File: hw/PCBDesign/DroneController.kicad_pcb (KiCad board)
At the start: 4 copper layers, 100 x 50 mm, 220 parts, among them J1 SerialDebug, J10 SW_B, J11 YTrim, J12 SW_C, J13 TTrim, J14 SW_D, J2 USB_B_Micro, J3 ExtBatt, J4 Conn_ARM_JTAG_SWD_10, J5 EncoderConn, J6 JoystickConn, J7 PTrim, J8 SW_A, J9 RTrim, Q1 MMBT3904, Q2 2N7002, Q3 2N7002, Q4 LBSS84LT1G, Q5 LBSS84LT1G, SW13 Key_User, SW15 Key_nRESET, SW17 Key_nBOOT, U1 74HC165, U11 74HC595, U13 STM32F446RETx, U14 RN4871, U2 74HC165, U3 74HC165, U4 AT25SF081, U5 AT24C256, U6 NRF24L01_Breakout, U7 TP4056, U8 AMS1117-3.3, Y1 8MHz Crystal

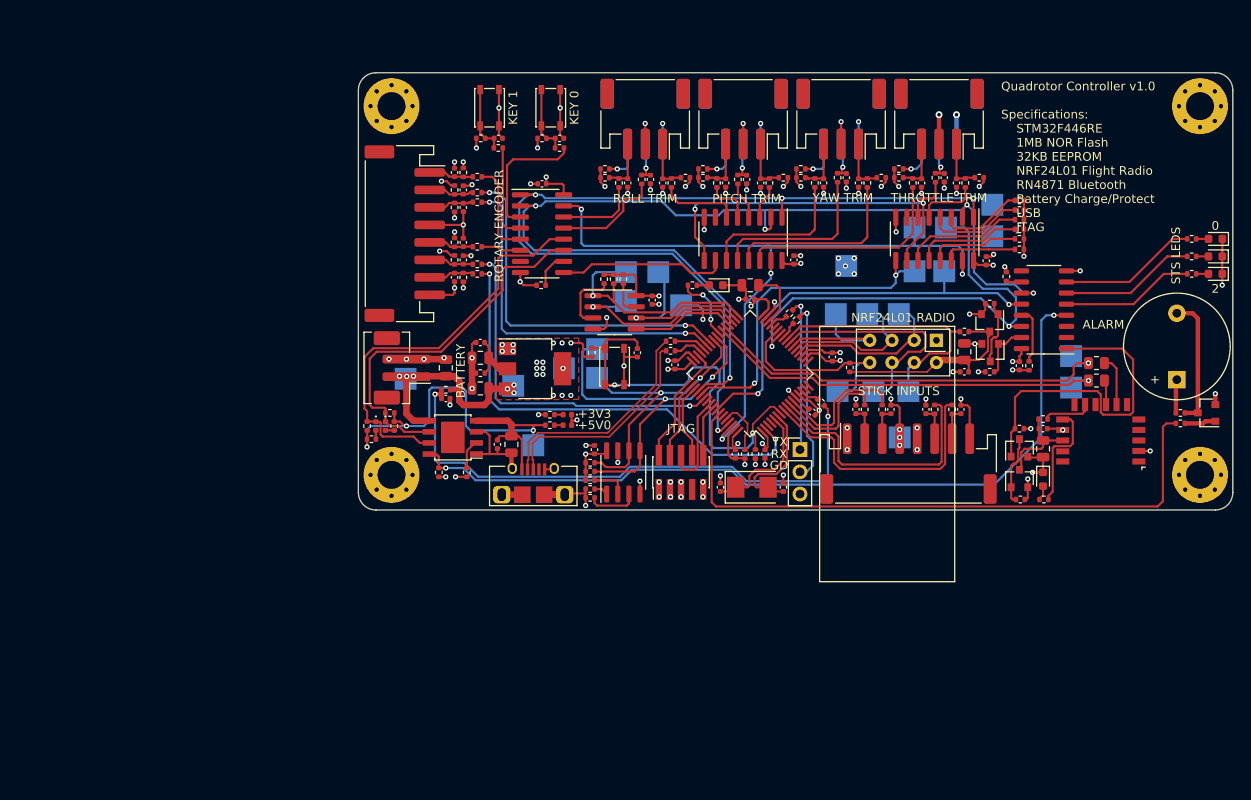
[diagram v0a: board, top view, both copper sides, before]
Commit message: Start working on PCB rev 2.0
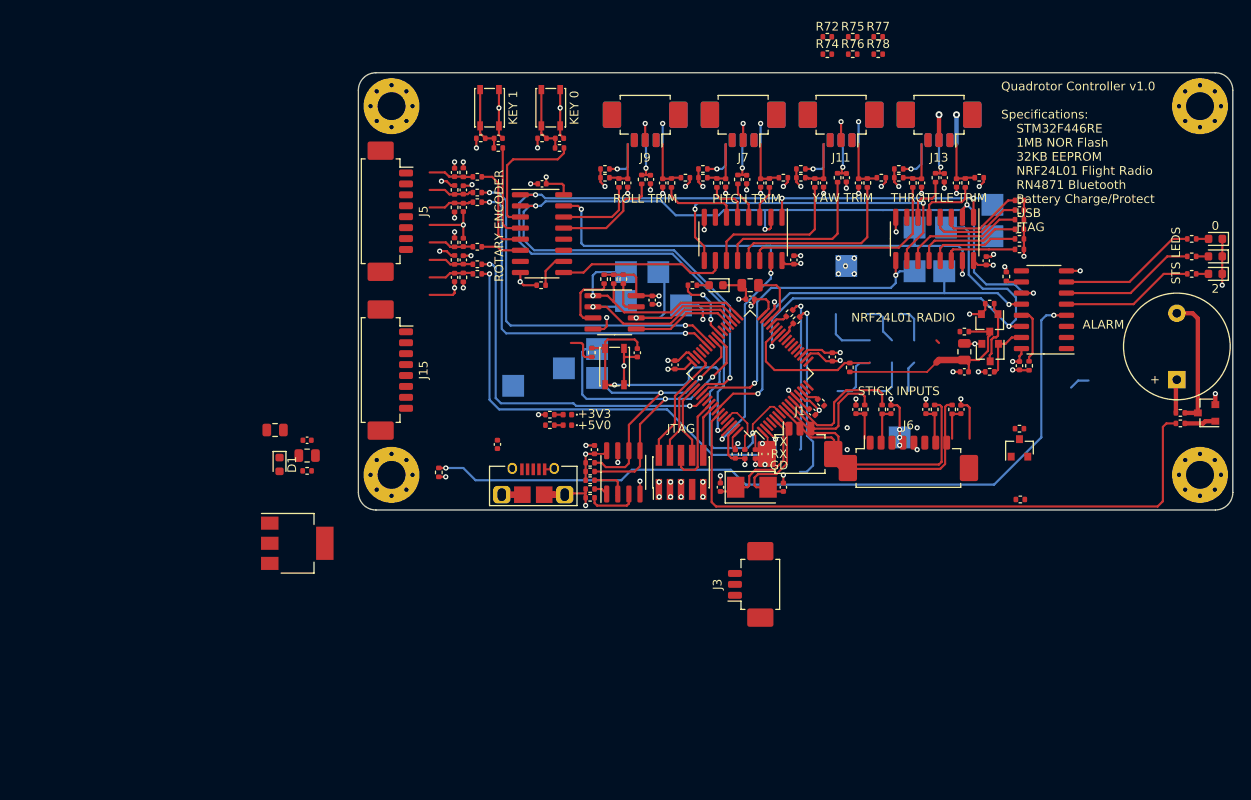
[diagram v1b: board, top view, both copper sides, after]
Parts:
- removed C36: 1uF, Capacitor_SMD:C_0805_2012Metric
- removed C38: 4.7uF, Capacitor_SMD:C_0805_2012Metric
- removed C40, C58: 100n, Capacitor_SMD:C_0402_1005Metric
- removed C59: 10uF, Capacitor_SMD:C_0805_2012Metric
- removed D2: LED_CHG, LED_SMD:LED_0402_1005Metric
- removed D7: BT_ON, LED_SMD:LED_0603_1608Metric
- removed Q4: LBSS84LT1G, Package_TO_SOT_SMD:SOT-23
- removed R100, R79: 10k, Resistor_SMD:R_0402_1005Metric
- removed R101: 560, Resistor_SMD:R_0402_1005Metric
- removed R52, R54: 33, Resistor_SMD:R_0402_1005Metric
- removed R80, R81: 1.5k, Resistor_SMD:R_0402_1005Metric
- removed R82, R83, R84: 100k, Resistor_SMD:R_0402_1005Metric
- removed R86, R87: 0, Resistor_SMD:R_0805_2012Metric
- removed TP10, TP11, TP12, TP13, TP14, TP23, TP24, TP7, TP8, TP9: TestPoint, TestPoint:TestPoint_Pad_2.5x2.5mm
- removed U14: RN4871, RF_Module:Microchip_RN4871
- removed U6: NRF24L01_Breakout, RF_Module:nRF24L01_Breakout
- removed U7: TP4056, PMIC:TP4056_SOP-8-PP
- added J15: Conn_01x08, Connector_Molex:Molex_PicoBlade_53261-0871_1x08-1MP_P1.25mm_Horizontal, F.Cu at (113.0, 114.0)
- added R72: 10k, Resistor_SMD:R_0402_1005Metric, F.Cu at (163.6, 75.9)
- added R74: 10k, Resistor_SMD:R_0402_1005Metric, F.Cu at (163.6, 77.9)
- added R75: 1.5k, Resistor_SMD:R_0402_1005Metric, F.Cu at (166.5, 75.9)
- added R76: 4.7k, Resistor_SMD:R_0402_1005Metric, F.Cu at (166.5, 77.9)
- added R77: 33k, Resistor_SMD:R_0402_1005Metric, F.Cu at (169.4, 75.9)
- added R78: 100, Resistor_SMD:R_0402_1005Metric, F.Cu at (169.4, 77.9)
- D1: value LED_PGD -> DBG_LED_0; footprint LED_SMD:LED_0402_1005Metric -> LED_SMD:LED_0603_1608Metric
- D4: value DBG_LED_2 -> DBG_LED_3
- D5: value DBG_LED_1 -> DBG_LED_2
- D6: value DBG_LED_0 -> DBG_LED_1
- J1: footprint Connector_PinHeader_2.54mm:PinHeader_1x03_P2.54mm_Vertical -> Connector_Molex:Molex_PicoBlade_53261-0371_1x03-1MP_P1.25mm_Horizontal
- J10, J11, J12, J13, J14, J7, J8, J9: footprint Connector_JST:JST_PH_S3B-PH-SM4-TB_1x03-1MP_P2.00mm_Horizontal -> Connector_Molex:Molex_PicoBlade_53261-0371_1x03-1MP_P1.25mm_Horizontal
- J3: value ExtBatt -> SerialDebug; footprint Connector_JST:JST_PH_B2B-PH-SM4-TB_1x02-1MP_P2.00mm_Vertical -> Connector_Molex:Molex_PicoBlade_53261-0371_1x03-1MP_P1.25mm_Horizontal
- J5, J6: footprint Connector_JST:JST_PH_S8B-PH-SM4-TB_1x08-1MP_P2.00mm_Horizontal -> Connector_Molex:Molex_PicoBlade_53261-0871_1x08-1MP_P1.25mm_Horizontal
- Q2: value 2N7002 -> MMBT3904
- R56: value 10k -> 560
- R73: value 100k -> 5.1k
- moved J3 47.4 mm to (155.5, 138.5)
- moved U8 33.7 mm to (103.0, 133.8)
- moved C41 24.0 mm to (100.5, 120.9)
- moved C44 22.7 mm to (104.1, 123.8)
- moved C47 22.7 mm to (104.1, 122.0)
- moved R85 22.7 mm to (104.1, 125.5)
- moved D1 12.9 mm to (101.0, 124.8)
- moved J5 3.41 mm to (113.0, 95.8)
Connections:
- net /Processor/DBG_UART_RX renamed /Processor/DBG_UART_RX_0
- net /Processor/DBG_UART_TX renamed /Processor/DBG_UART_TX_0
- C41 pad 2: /Power Supply/vBatt -> +5V
- D1 pad 1: nBatteryPowerGood -> GND
- J2 pad 4: (no net) -> GND
- J3 pad 1: /Power Supply/vBatt -> /Processor/DBG_UART_TX_1
- J3 pad 2: GND -> /Processor/DBG_UART_RX_1
- J4 pad 7: (no net) -> Net-(J4-Pad7)
- Q2 pad 1: /Processor/BT_VCC_EN -> Net-(Q2-Pad1)
- Q2 pad 2: GND -> Net-(Q2-Pad2)
- Q2 pad 3: Net-(Q2-Pad3) -> +3V3
- R56 pad 1: GND -> Net-(D1-Pad2)
- R56 pad 2: /Processor/BT_VCC_EN -> Net-(R56-Pad2)
- R59 pad 1: Net-(Q2-Pad3) -> Net-(R59-Pad1)
- R59 pad 2: +3V3 -> /Processor/DBG_UART_RX_1
- R65 pad 1: /Processor/VSense_Batt -> Net-(R65-Pad1)
- R65 pad 2: Net-(R65-Pad2) -> /Processor/DBG_UART_TX_1
- R73 pad 1: /Power Supply/CHG_nEN -> /Processor/USB_SENSE
- R73 pad 2: GND -> +5V
- TP25 pad 1: /Power Supply/vBatt -> +5V
- U1 pad 7: (no net) -> Net-(U1-Pad7)
- U11 pad 1: /Processor/BT_VCC_EN -> /Processor/USB_nRENUMERATE
- U11 pad 2: (no net) -> Net-(U11-Pad2)
- U11 pad 3: (no net) -> Net-(U11-Pad3)
- U11 pad 4: /Power Supply/CHG_nEN -> Net-(R56-Pad2)
- U11 pad 9: (no net) -> Net-(U11-Pad9)
- U13 pad 14: Net-(R65-Pad2) -> Net-(U13-Pad14)
- U13 pad 15: (no net) -> Net-(U13-Pad15)
- U13 pad 16: (no net) -> /Human Machine Interface/ENC1_A
- U13 pad 17: (no net) -> /Human Machine Interface/ENC1_B
- U13 pad 28: (no net) -> Net-(U13-Pad28)
- U13 pad 3: (no net) -> Net-(U13-Pad3)
- U13 pad 37: /Wireless/BT_RX -> Net-(R65-Pad1)
- U13 pad 38: /Wireless/BT_TX -> Net-(R59-Pad1)
- U13 pad 4: (no net) -> Net-(U13-Pad4)
- U13 pad 42: /Human Machine Interface/ENC1_A -> /Processor/USB_SENSE
- U13 pad 43: /Human Machine Interface/ENC1_B -> /Processor/USB_ID
- U13 pad 44: Net-(R52-Pad2) -> /Power Supply/USB_D-
- U13 pad 45: Net-(R54-Pad2) -> /Power Supply/USB_D+
- U13 pad 54: (no net) -> Net-(U13-Pad54)
- U13 pad 59: (no net) -> Net-(U13-Pad59)
- U2 pad 7: (no net) -> Net-(U2-Pad7)
- U3 pad 11: nBatteryPowerGood -> /Human Machine Interface/d0
- U3 pad 12: nBatteryChargeGood -> /Human Machine Interface/d1
- U3 pad 7: (no net) -> Net-(U3-Pad7)
- U8 pad 3: /Power Supply/vBatt -> +5V
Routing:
- net /Processor/VSense_Batt: track 64.6 -> 0.00 mm, vias 2 -> 0
- net +5V: track 53.6 -> 0.79 mm, vias 3 -> 1
- net /Wireless/BT_RX: track 47.6 -> 0.00 mm, vias 1 -> 0
- net /Wireless/BT_TX: track 46.9 -> 0.00 mm, vias 1 -> 0
- net nBatteryChargeGood: track 46.8 -> 0.00 mm
- net nBatteryPowerGood: track 43.0 -> 0.00 mm
- net /Processor/BT_VCC_EN: track 37.5 -> 0.00 mm
- net GND: track 182.0 -> 147.9 mm, vias 93 -> 75
- net /Processor/RF24_nCS: track 31.2 -> 3.53 mm
- net /Power Supply/USB_D-: track 25.9 -> 0.00 mm
- net /Power Supply/USB_D+: track 24.9 -> 0.00 mm
- net /Power Supply/vBatt: track 24.1 -> 0.00 mm, vias 6 -> 0
- net /Processor/RF24_MOSI: track 27.3 -> 5.08 mm
- net /Processor/RF24_CE: track 18.9 -> 4.43 mm
- net Net-(R101-Pad2): track 12.4 -> 0.00 mm
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- removed copper zone on F.Cu, net +3V3
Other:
- board text removed: "BATTERY"

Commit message: Add more work on PCB v2 design
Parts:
- removed TP1, TP15, TP16, TP17, TP18, TP19, TP2, TP20, TP21, TP22, TP25, TP26, TP3, TP4, TP5, TP6: TestPoint, TestPoint:TestPoint_Pad_2.5x2.5mm
- added R52: 10k, Resistor_SMD:R_0402_1005Metric, F.Cu at (72.8, 98.4)
- added R54: 10k, Resistor_SMD:R_0402_1005Metric, F.Cu at (75.7, 98.4)
- J3: moved to B.Cu
- moved Q3 96.3 mm to (86.3, 120.3)
- moved Q5 95.0 mm to (87.6, 116.9)
- moved C34 90.6 mm to (89.3, 122.4)
- moved C35 90.6 mm to (89.3, 124.7)
- moved R70 90.6 mm to (89.3, 120.1)
- moved R58 90.6 mm to (92.2, 124.7)
- moved R98 90.6 mm to (92.2, 116.9)
- moved C52 68.8 mm to (90.0, 127.7)
- moved C55 68.8 mm to (90.0, 129.3)
- moved D3 68.8 mm to (86.1, 127.7)
- moved R92 68.8 mm to (83.4, 127.7)
- moved H4 50.2 mm to (156.0, 126.0)
- moved H3 50.1 mm to (156.1, 83.8)
- moved C2 48.8 mm to (151.7, 149.5)
- moved U11 43.1 mm to (146.6, 117.4)
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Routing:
- net /Human Machine Interface/KEY_SCK: track 121.6 -> 1.75 mm, vias 5 -> 1
- net /Human Machine Interface/KEY_nSAMPLE: track 108.1 -> 1.73 mm, vias 4 -> 1
- net /Power Supply/CHG_nEN: track 89.4 -> 0.00 mm, vias 2 -> 0
- net /Human Machine Interface/KEY_nCS: track 84.9 -> 1.65 mm, vias 4 -> 0
- net GND: track 147.9 -> 72.3 mm, vias 75 -> 34
- net /Human Machine Interface/PWM_Buzzer: track 72.7 -> 0.00 mm
- net /Processor/KEY_MOSI: track 53.6 -> 0.00 mm, vias 2 -> 0
- net /Human Machine Interface/ENC0_B: track 53.7 -> 0.89 mm, vias 2 -> 1
- net /Processor/KeyOut_nCS: track 48.1 -> 0.00 mm, vias 2 -> 0
- net +3V3: track 82.7 -> 38.0 mm, vias 38 -> 18
- net /Processor/EEPROM_SDA: track 42.9 -> 0.00 mm, vias 2 -> 0
- net /Human Machine Interface/ENC1_A: track 41.4 -> 0.89 mm, vias 2 -> 1
- net /Human Machine Interface/ENC0_A: track 41.3 -> 0.89 mm, vias 2 -> 1
- net Net-(U1-Pad10): track 40.3 -> 0.00 mm, vias 2 -> 0
- net /Human Machine Interface/ENC1_B: track 40.8 -> 0.89 mm, vias 2 -> 1
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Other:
- board size 100 x 50 mm -> 50 x 50 mm
- board text added: "ROTARY ENCODERS"
- board text removed: "3V3"
- board text removed: "5V0"
- board text removed: "Analog Ground"
- board text removed: "BATT"
- board text removed: "BATT_PROTECT"
- board text removed: "Bluetooth"
- board text removed: "CE"
- board text removed: "CS"
- board text removed: "CS_IN"
- board text removed: "CS_OUT"
- board text removed: "Digital Ground"
- board text removed: "Digital IO Shift Registers"
- board text removed: "EEPROM"
- board text removed: "IRQ"
- board text removed: "MISO"
- board text removed: "MOSI"
- board text removed: "NOR Flash Memory"
- board text removed: "ROTARY ENCODER"
- board text removed: "RX"
- board text removed: "SCK"
- board text removed: "SCL"
- board text removed: "SDA"
- board text removed: "STRB"
- board text removed: "TX"

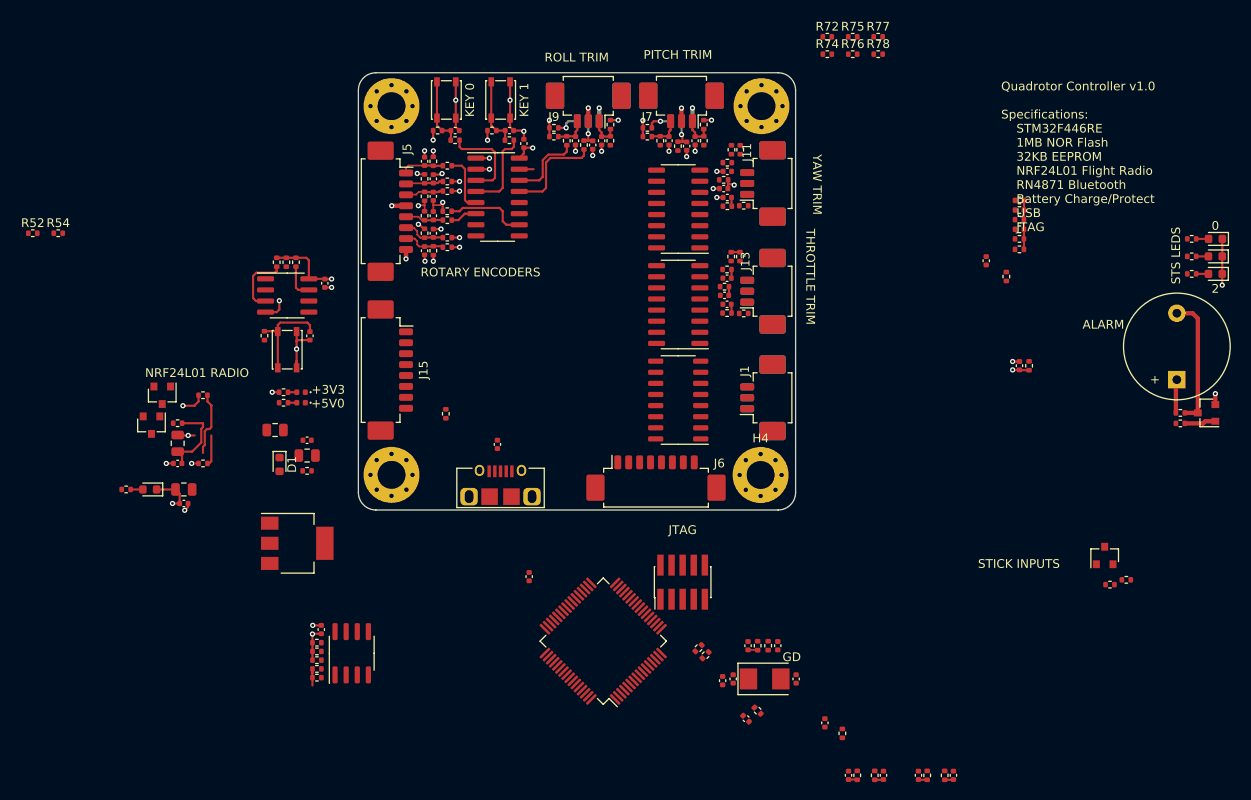
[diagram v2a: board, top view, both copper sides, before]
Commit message: Work further on v2.0 of controller pcb
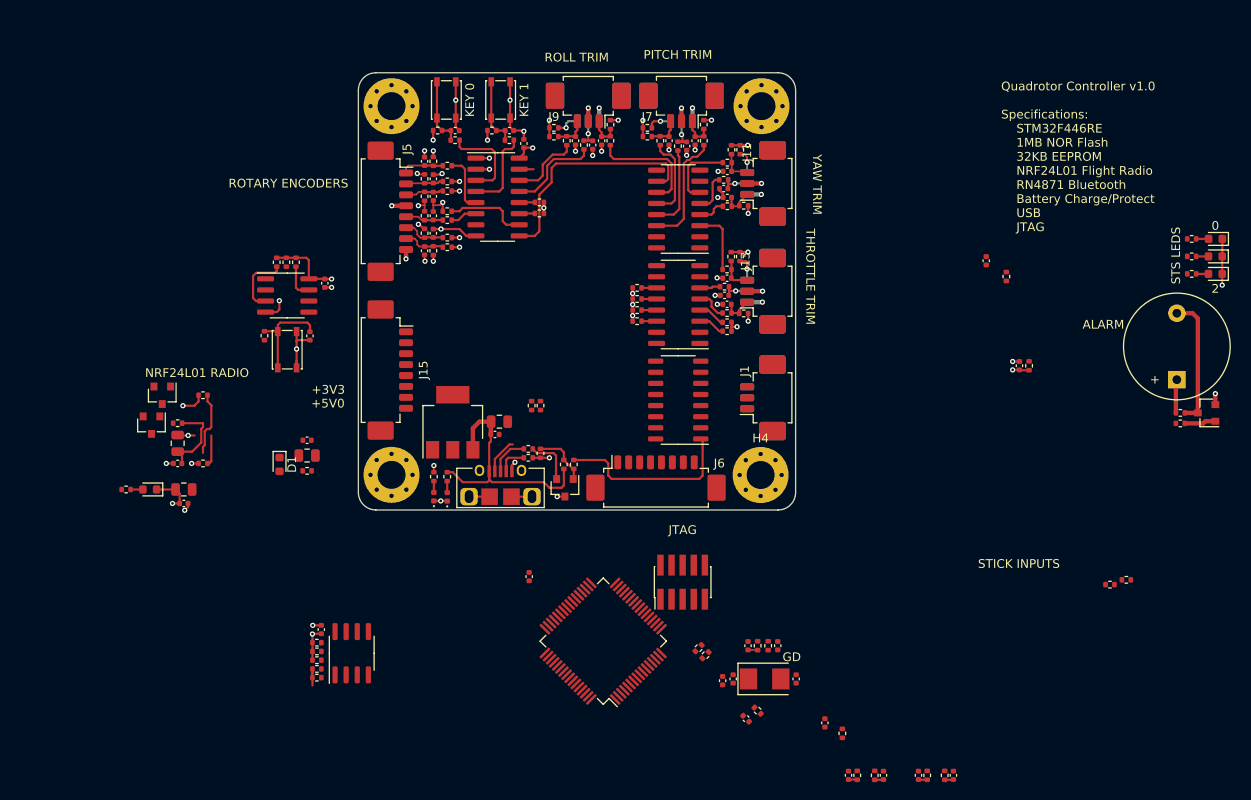
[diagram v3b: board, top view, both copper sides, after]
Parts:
- moved Q2 62.2 mm to (133.6, 127.5), turned to 270 degrees
- moved R77 61.3 mm to (130.8, 123.5), turned to 90 degrees
- moved R75 60.0 mm to (129.4, 123.0)
- moved R72 59.1 mm to (129.4, 124.0), turned to 180 degrees
- moved R78 58.4 mm to (134.6, 124.8), turned to 270 degrees
- moved R52 58.0 mm to (130.7, 94.8)
- moved R76 57.4 mm to (133.5, 124.8), turned to 270 degrees
- moved R54 55.1 mm to (130.7, 96.1)
- moved R74 52.5 mm to (129.8, 118.1), turned to 90 degrees
- moved R51 44.5 mm to (141.9, 108.4), turned to 180 degrees
- moved R47 44.5 mm to (141.9, 107.1), turned to 180 degrees
- moved R2 44.4 mm to (141.9, 105.9), turned to 180 degrees
- moved R49 44.4 mm to (141.9, 104.6), turned to 180 degrees
- moved R46 36.6 mm to (152.2, 109.6)
- moved R45 35.8 mm to (152.2, 108.5)
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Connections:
- J2 pad 4: GND -> /Power Supply/USB_ID
- R18 pad 1: /Human Machine Interface/d14 -> /Human Machine Interface/d9
- R19 pad 2: /Human Machine Interface/d12 -> /Human Machine Interface/d11
- R21 pad 2: /Human Machine Interface/d9 -> /Human Machine Interface/d14
- R26 pad 2: /Human Machine Interface/d15 -> /Human Machine Interface/d8
- R27 pad 2: /Human Machine Interface/d13 -> /Human Machine Interface/d10
- R31 pad 1: /Human Machine Interface/d8 -> /Human Machine Interface/d15
- R32 pad 2: /Human Machine Interface/d10 -> /Human Machine Interface/d13
- R37 pad 1: /Human Machine Interface/d11 -> /Human Machine Interface/d12
- R72 pad 2: /Processor/USB_ID -> /Power Supply/USB_ID
- U13 pad 43: /Processor/USB_ID -> /Power Supply/USB_ID
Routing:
- net +5V: track 0.00 -> 28.9 mm
- net Net-(U2-Pad10): track 0.00 -> 27.0 mm
- net GND: track 72.3 -> 95.5 mm, vias 34 -> 48
- net /Processor/USB_nRENUMERATE: track 0.00 -> 20.9 mm
- net /Human Machine Interface/d8: track 0.00 -> 13.4 mm
- net /Human Machine Interface/d11: track 0.00 -> 13.3 mm
- net /Human Machine Interface/d9: track 0.00 -> 9.67 mm
- net /Human Machine Interface/d10: track 0.00 -> 9.61 mm
- net /Human Machine Interface/d15: track 0.00 -> 8.34 mm
- net /Human Machine Interface/d12: track 0.00 -> 7.39 mm
- net Net-(Q2-Pad1): track 0.00 -> 6.46 mm
- net Net-(Q2-Pad2): track 0.00 -> 5.69 mm
- net +3V3: track 38.0 -> 43.4 mm, vias 18 -> 23
- net /Power Supply/USB_D+: track 0.00 -> 4.56 mm
- net /Human Machine Interface/d14: track 0.00 -> 4.53 mm
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
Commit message: Improve PCB design
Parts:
- removed C53, C54: 1.5pF, Capacitor_SMD:C_0402_1005Metric
- removed Y1: 8MHz Crystal, Crystal:Crystal_SMD_5032-2Pin_5.0x3.2mm
- U4: moved to B.Cu
- moved R61 68.1 mm to (141.9, 91.8), turned to 0 degrees
- moved R66 66.4 mm to (141.9, 92.8), turned to 180 degrees
- moved R62 64.8 mm to (141.9, 93.8), turned to 180 degrees
- moved R68 63.1 mm to (141.9, 94.8), turned to 180 degrees
- moved R59 62.0 mm to (138.8, 114.6)
- moved R69 61.5 mm to (141.9, 95.8), turned to 180 degrees
- moved R71 61.4 mm to (117.4, 117.1), turned to 180 degrees
- moved U5 59.4 mm to (138.3, 94.5), turned to 270 degrees
- moved C27 58.5 mm to (141.4, 97.3), turned to 270 degrees
- moved D6 58.3 mm to (151.7, 118.1)
- moved D5 58.1 mm to (151.7, 115.5)
- moved D4 58.0 mm to (151.7, 113.0)
- moved R95 55.3 mm to (151.7, 116.8)
- moved R94 55.2 mm to (151.7, 114.3)
- moved R93 55.1 mm to (151.7, 111.8)
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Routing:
- net /Processor/RF24_VCC_EN: track 3.49 -> 65.4 mm
- net /Human Machine Interface/Joy Stick Inputs/JS_0: track 1.01 -> 13.5 mm
- net /Human Machine Interface/Joy Stick Inputs/JS_2: track 1.01 -> 11.3 mm
- net /Human Machine Interface/Joy Stick Inputs/JS_3: track 1.01 -> 10.5 mm
- net GND: track 95.5 -> 104.6 mm, vias 48 -> 68
- net /Human Machine Interface/Joy Stick Inputs/JS_1: track 1.01 -> 9.46 mm
- net Net-(R67-Pad2): track 7.52 -> 0.00 mm
- net /Processor/EEPROM_SDA: track 0.00 -> 7.08 mm
- net +3V3: track 43.4 -> 49.2 mm, vias 23 -> 36
- net /Processor/EEPROM_SCL: track 0.00 -> 5.67 mm
- net Net-(R61-Pad1): track 0.00 -> 5.64 mm
- net +5V: track 28.9 -> 23.3 mm
- net /Human Machine Interface/nRESET: track 11.2 -> 6.49 mm
- net Net-(R93-Pad2): track 0.00 -> 4.24 mm
- net Net-(R62-Pad2): track 0.00 -> 4.06 mm
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- removed copper zone on In2.Cu, net /Power Supply/vBatt
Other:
- board text removed: "0"
- board text removed: "2"
- board text removed: "GD"
